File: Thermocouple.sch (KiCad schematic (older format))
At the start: 0 parts

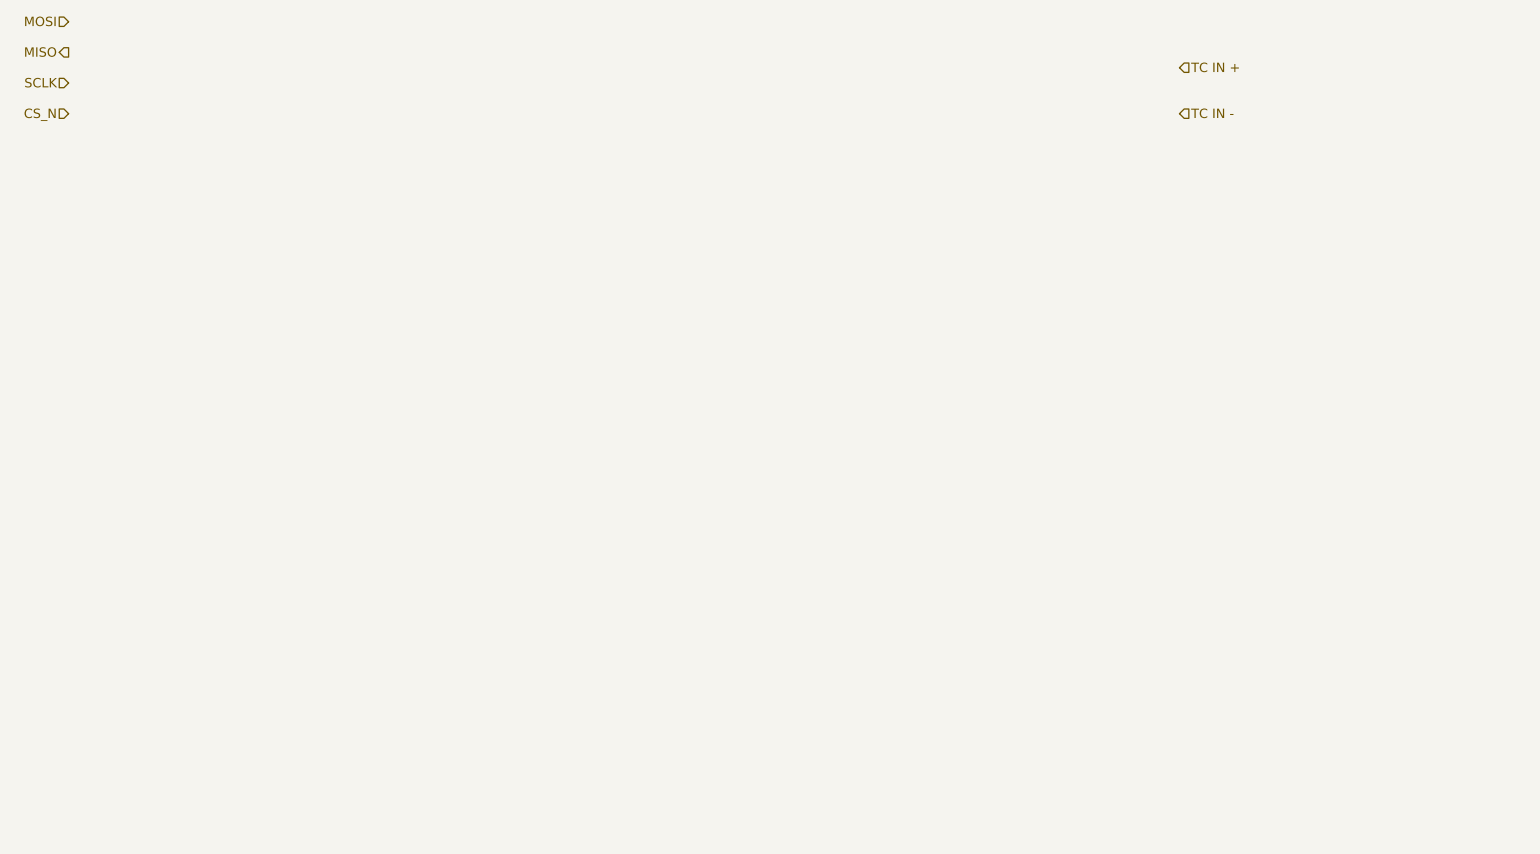
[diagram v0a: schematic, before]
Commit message: Thermocouple Rough Schematic
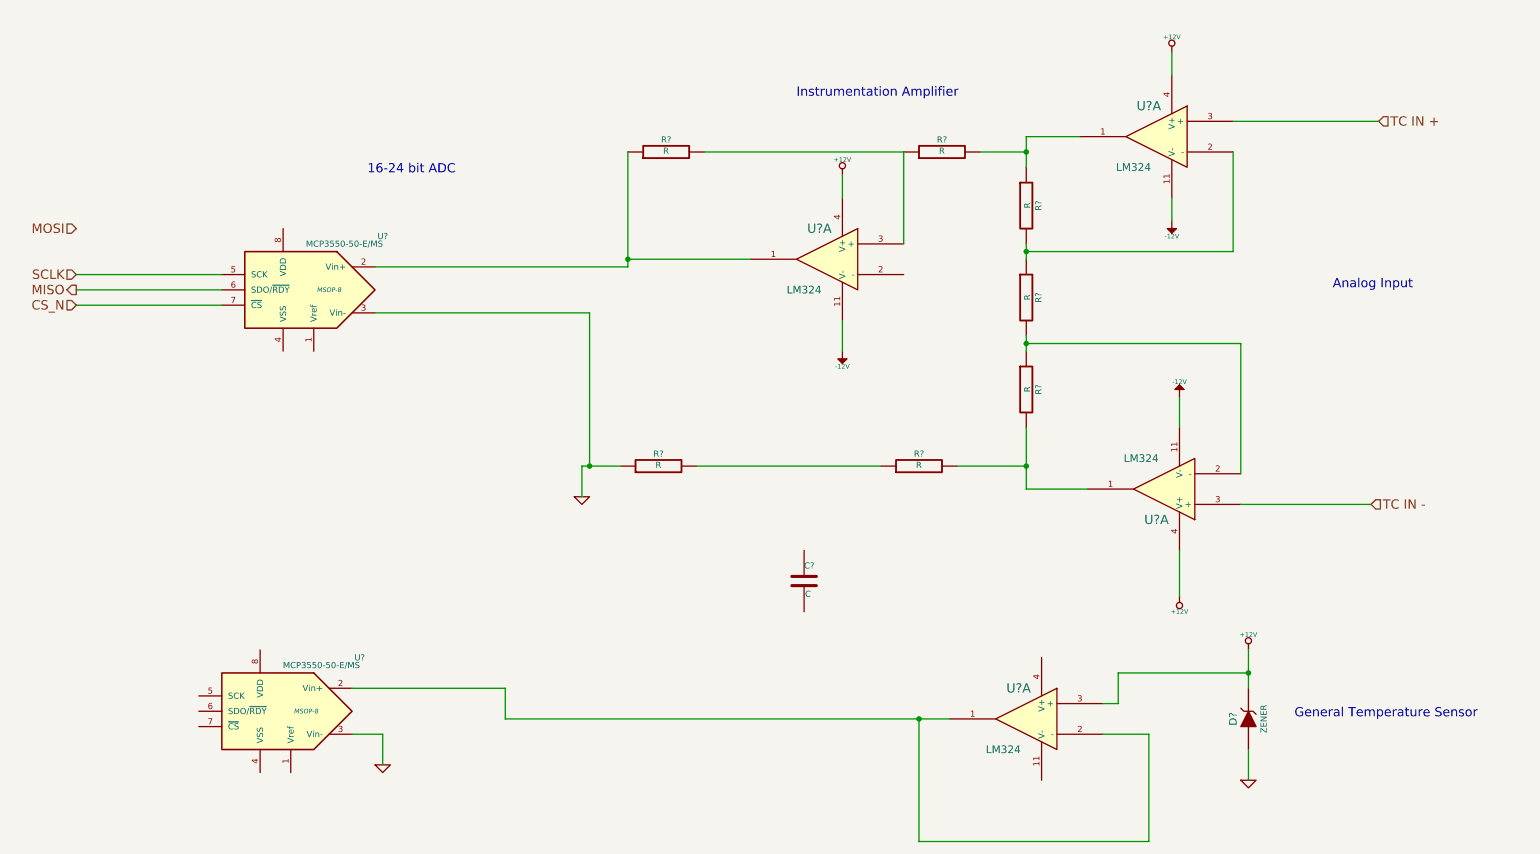
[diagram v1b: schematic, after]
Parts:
- added C?: C, ~, symbol C
- added D?: ZENER, ~, symbol ZENER
- added R? (x7): R, ~, symbol R
- added U? (x4): LM324, symbol LM324
- added U? (x2): MCP3550-50-E/MS, MSOP-8, symbol MCP3550-50-E/MS
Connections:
- net CS_N: now also U?.7 (~CS~)
- net MISO: now also U?.6 (SDO/~RDY~)
- net SCLK: now also U?.5 (SCK)
- net TC IN +: now also U?.3 (+)
- net TC IN -: now also U?.3 (+)
- new net: R?.1, U?.1, U?.2 (Vin+)
- new net: R?.1, R?.2, U?.3 (+)
- new net: R?.1, R?.2, U?.1
- new net: R?.1, R?.2, U?.2 (-) (x2)
- new net: R?.2, R?.2, U?.1
- new net: U?.1, U?.2 (-), U?.2 (Vin+)
- new net: R?.1, R?.2
- new net +12V: D?.2 (K), U?.3 (+), U?.4 (V+), U?.4 (V+), U?.4 (V+)
- new net -12V: U?.11 (V-), U?.11 (V-), U?.11 (V-)
- new net GND: D?.1 (A), R?.1, U?.3 (Vin-), U?.3 (Vin-)
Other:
- note added: "16-24 bit ADC"
- note added: "Analog Input"
- note added: "General Temperature Sensor"
- note added: "Instrumentation Amplifier"
